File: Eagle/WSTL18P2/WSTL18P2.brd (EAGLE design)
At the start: 23.2 x 23.2 mm, 22 parts, among them CON1 1X6CONN-1.27-ROUND, CON2 1X6CONN-1.27-ROUND, CON3 1X6CONN-1.27-ROUND, CON4 1X6CONN-1.27-ROUND, T1 ABS07AIG

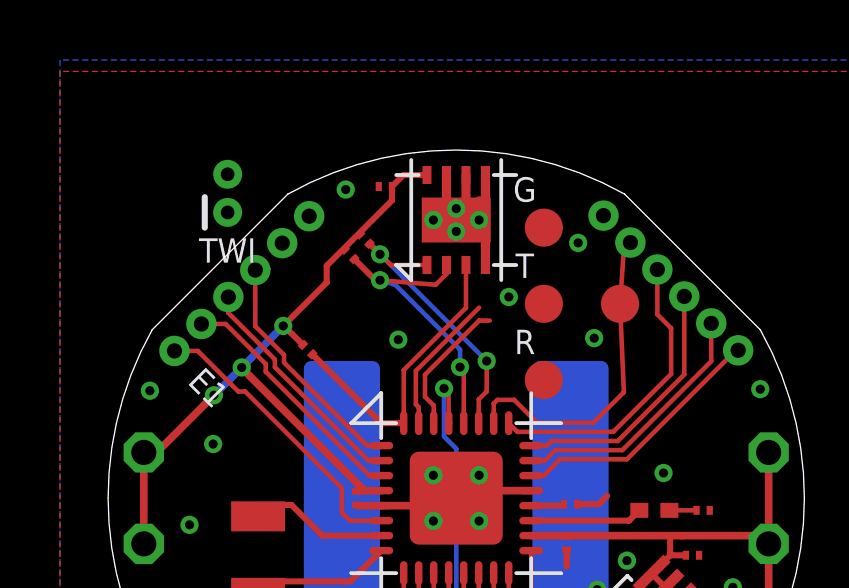
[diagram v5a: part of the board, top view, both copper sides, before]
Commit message: Made TWI (I2C) available on perimeter 1.27mm headers
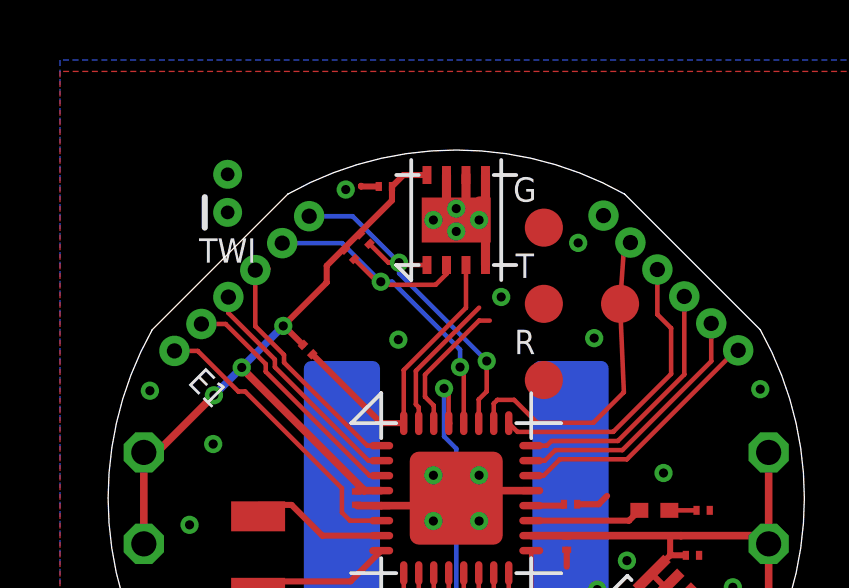
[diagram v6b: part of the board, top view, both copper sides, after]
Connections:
- net SCL0: now also CON4.2
- net SDA0: now also CON4.1
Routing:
- net SCL0: track 9.91 -> 13.8 mm
- net SDA0: track 9.42 -> 12.5 mm
- net GND: track 13.7 -> 14.3 mm
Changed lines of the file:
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@@
 <wire x1="7.3152" y1="17.8054" x2="7.3152" y2="17.7038" width="0.1524" layer="51"/>
 <wire x1="6.8072" y1="18.415" x2="6.9342" y2="18.288" width="0.1524" layer="51"/>
-<wire x1="10.795" y1="20.9042" x2="10.5156" y2="20.9042" width="0.254" layer="51"/>
+<wire x1="11.303" y1="20.447" x2="11.049" y2="20.701" width="0.254" layer="51"/>
 </plain>
 <attributes>
@@
 <contactref element="R2" pad="2"/>
 <via x="14.224" y="17.78" extent="1-16" drill="0.3048" shape="octagon"/>
-<wire x1="14.224" y1="17.78" x2="10.668" y2="21.336" width="0.1524" layer="16"/>
-<wire x1="12.233" y1="20.979" x2="11.025" y2="20.979" width="0.1524" layer="1"/>
+<wire x1="14.224" y1="17.78" x2="11.303" y2="20.701" width="0.1524" layer="16"/>
 <wire x1="13.958" y1="15.708" x2="13.958" y2="16.498" width="0.1524" layer="1"/>
 <wire x1="13.958" y1="16.498" x2="14.224" y2="16.764" width="0.1524" layer="1"/>
 <wire x1="14.224" y1="16.764" x2="14.224" y2="17.78" width="0.1524" layer="1"/>
-<via x="10.668" y="21.336" extent="1-16" drill="0.3048" shape="octagon"/>
-<wire x1="10.668" y1="21.336" x2="11.025" y2="20.979" width="0.1524" layer="1"/>
-<wire x1="10.668" y1="21.336" x2="10.315565625" y2="21.688434375" width="0.2032" layer="1"/>
+<via x="11.303" y="21.0566" extent="1-16" drill="0.3048" shape="octagon"/>
 <wire x1="10.315565625" y1="21.688434375" x2="10.3155625" y2="21.688434375" width="0.2032" layer="1"/>
+<contactref element="CON4" pad="1"/>
+<wire x1="12.233" y1="20.979" x2="11.3806" y2="20.979" width="0.1524" layer="1"/>
+<wire x1="11.3806" y1="20.979" x2="11.303" y2="21.0566" width="0.1524" layer="1"/>
+<wire x1="11.303" y1="20.701" x2="11.303" y2="21.0566" width="0.1524" layer="16"/>
+<wire x1="11.303" y1="21.0566" x2="9.7536" y2="22.606" width="0.1524" layer="16"/>
+<wire x1="9.7536" y1="22.606" x2="8.3058" y2="22.606" width="0.1524" layer="16"/>
+<wire x1="10.3155625" y1="21.688434375" x2="10.947396875" y2="21.0566" width="0.1524" layer="1"/>
+<wire x1="10.947396875" y1="21.0566" x2="11.303" y2="21.0566" width="0.1524" layer="1"/>
 </signal>
 <signal name="SCL0" class="2">
@@
 <contactref element="TMP" pad="2"/>
 <wire x1="13.458" y1="15.708" x2="13.458" y2="17.4538" width="0.1524" layer="1"/>
-<wire x1="12.883" y1="20.6808" x2="12.883" y2="20.979" width="0.1524" layer="1"/>
 <contactref element="R3" pad="2"/>
 <wire x1="13.458" y1="17.4538" x2="13.335" y2="17.5768" width="0.1524" layer="1"/>
 <via x="13.335" y="17.5768" extent="1-16" drill="0.3048" shape="octagon"/>
 <wire x1="13.335" y1="17.5768" x2="13.335" y2="18.161" width="0.1524" layer="16"/>
-<wire x1="13.335" y1="18.161" x2="11.176" y2="20.32" width="0.1524" layer="16"/>
-<wire x1="12.5222" y1="20.32" x2="12.883" y2="20.6808" width="0.1524" layer="1"/>
-<via x="10.668" y="20.4724" extent="1-16" drill="0.3048" shape="octagon"/>
-<wire x1="10.668" y1="20.4724" x2="11.176" y2="20.32" width="0.1524" layer="16"/>
-<wire x1="12.5222" y1="20.32" x2="10.668" y2="20.4724" width="0.1524" layer="1"/>
-<wire x1="10.668" y1="20.4724" x2="10.515596875" y2="20.4724" width="0.2032" layer="1"/>
-<wire x1="10.515596875" y1="20.4724" x2="9.8075625" y2="21.180434375" width="0.2032" layer="1"/>
+<wire x1="13.335" y1="18.161" x2="11.0744" y2="20.4216" width="0.1524" layer="16"/>
+<via x="10.6934" y="20.4216" extent="1-16" drill="0.3048" shape="octagon"/>
+<contactref element="CON4" pad="2"/>
+<wire x1="12.883" y1="20.979" x2="12.883" y2="20.6808" width="0.1524" layer="1"/>
+<wire x1="12.883" y1="20.6808" x2="12.5222" y2="20.32" width="0.1524" layer="1"/>
+<wire x1="12.5222" y1="20.32" x2="10.795" y2="20.32" width="0.1524" layer="1"/>
+<wire x1="10.795" y1="20.32" x2="10.6934" y2="20.4216" width="0.1524" layer="1"/>
+<wire x1="11.0744" y1="20.4216" x2="10.6934" y2="20.4216" width="0.1524" layer="16"/>
+<wire x1="10.6934" y1="20.4216" x2="9.407028125" y2="21.707971875" width="0.1524" layer="16"/>
+<wire x1="9.407028125" y1="21.707971875" x2="7.407771875" y2="21.707971875" width="0.1524" layer="16"/>
+<wire x1="9.8075625" y1="21.180434375" x2="10.566396875" y2="20.4216" width="0.1524" layer="1"/>
+<wire x1="10.566396875" y1="20.4216" x2="10.6934" y2="20.4216" width="0.1524" layer="1"/>
 </signal>
 <signal name="RESET" class="2">
@@
 <wire x1="13.97" y1="13.458" x2="13.97" y2="13.97" width="0.254" layer="1"/>
 <via x="6.9088" y="8.3312" extent="1-16" drill="0.3048"/>
-<via x="14.9606" y="19.9136" extent="1-16" drill="0.3048"/>
+<via x="14.7066" y="19.9136" extent="1-16" drill="0.3048"/>
 <wire x1="12.446" y1="12.958" x2="12.696" y2="13.208" width="0.254" layer="1"/>
 <wire x1="12.696" y1="13.208" x2="13.208" y2="13.208" width="0.254" layer="1"/>
@@
 <wire x1="9.9106" y1="12.958" x2="10.708" y2="12.958" width="0.254" layer="1"/>
 <wire x1="9.8806" y1="12.988" x2="9.9106" y2="12.958" width="0.2032" layer="1"/>
-<wire x1="9.525" y1="23.495" x2="10.6258" y2="23.5966" width="0" layer="19" extent="1-1"/>
-<wire x1="21.302" y1="11.303" x2="22.4282" y2="10.2362" width="0" layer="19" extent="1-1"/>
-<wire x1="21.6576" y1="12.8016" x2="21.302" y2="11.303" width="0" layer="19" extent="1-1"/>
+<wire x1="10.6258" y1="23.5966" x2="10.033" y2="23.5966" width="0.2032" layer="1"/>
+<wire x1="10.033" y1="23.5966" x2="10.033" y2="23.622" width="0.2032" layer="1"/>
+<wire x1="21.302" y1="11.303" x2="21.6576" y2="12.8016" width="0" layer="19" extent="1-1"/>
+<wire x1="22.4282" y1="10.2362" x2="21.302" y2="11.303" width="0" layer="19" extent="1-1"/>
 </signal>
 <signal name="AREF">

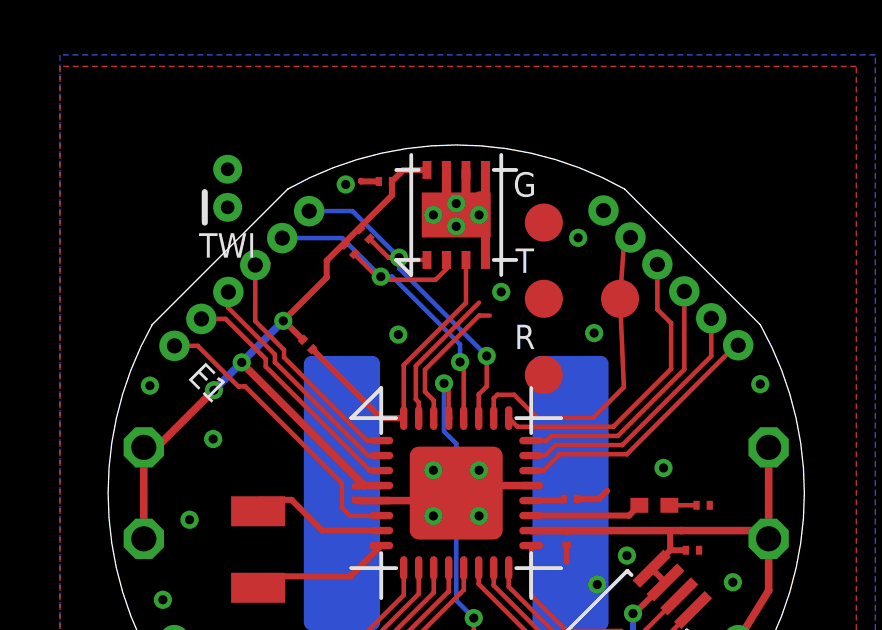
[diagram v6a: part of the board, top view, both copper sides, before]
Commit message: More work on TWI (I2C) traces
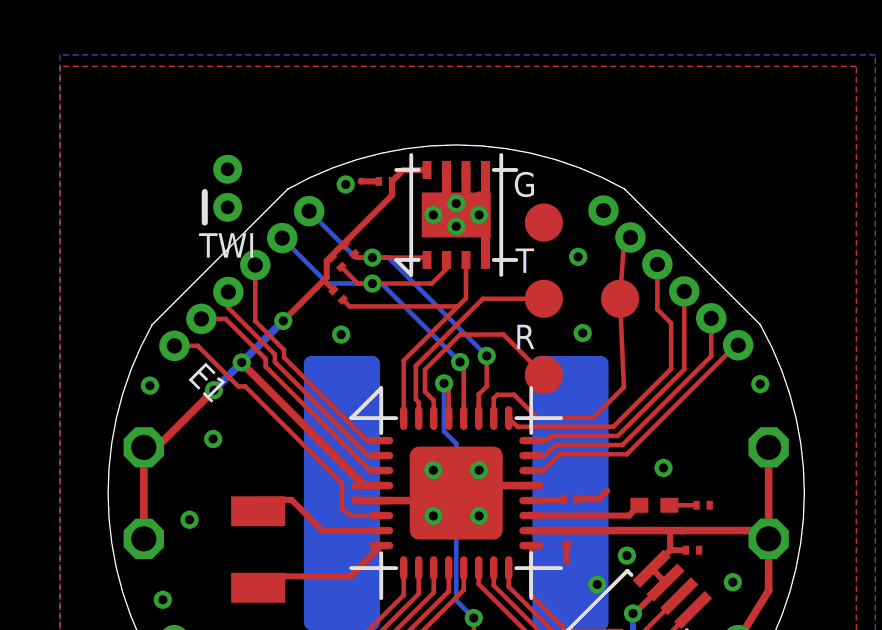
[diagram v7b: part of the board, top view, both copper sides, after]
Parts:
- moved R4 1.94 mm to (9.27, 19.8)
- moved R2 0.72 mm to (9.65, 21.3)
- moved R3 0.61 mm to (9.22, 20.9)
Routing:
- net TXD0: track 4.76 -> 6.97 mm
- net RXD0: track 4.64 -> 6.74 mm
- net GND: vias 27 -> 26

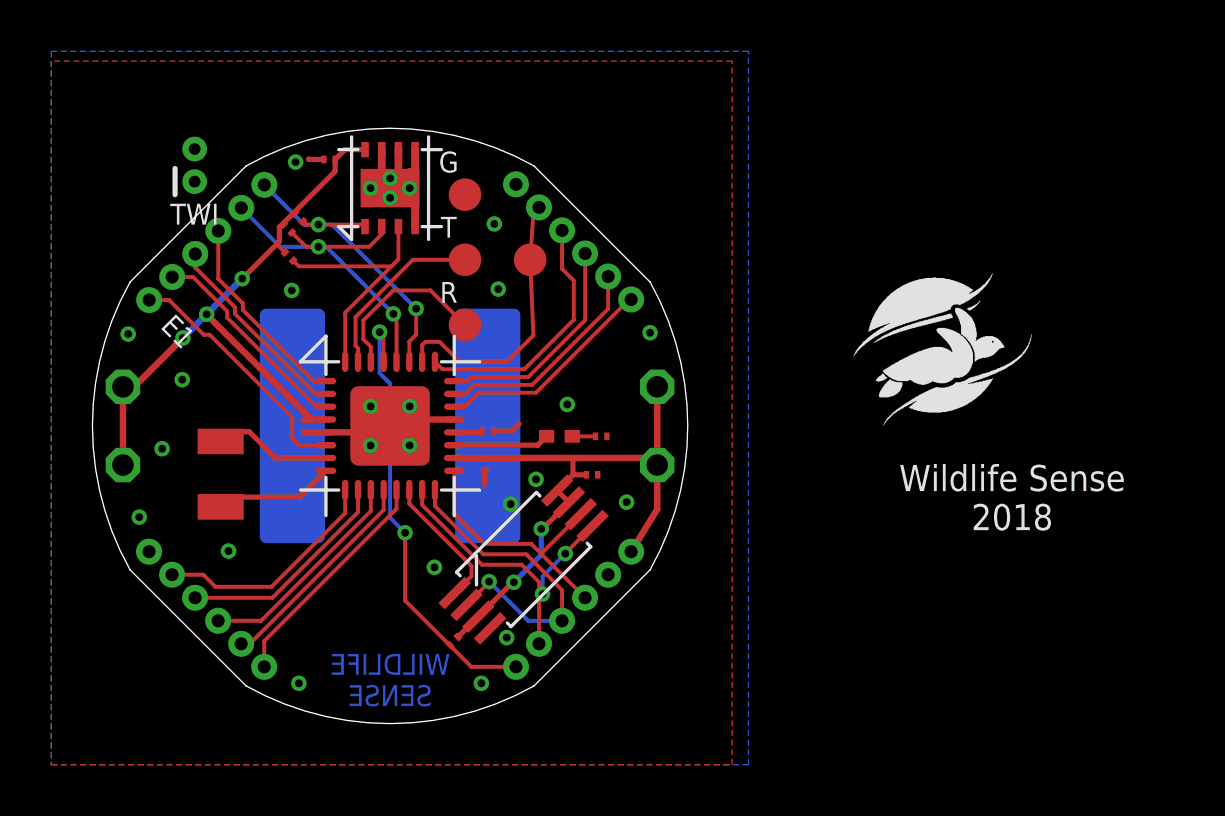
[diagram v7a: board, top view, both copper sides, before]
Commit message: Added pads on the positive battery holder contacts
This will allow use of both SMD and through-hole versions of the battery holder
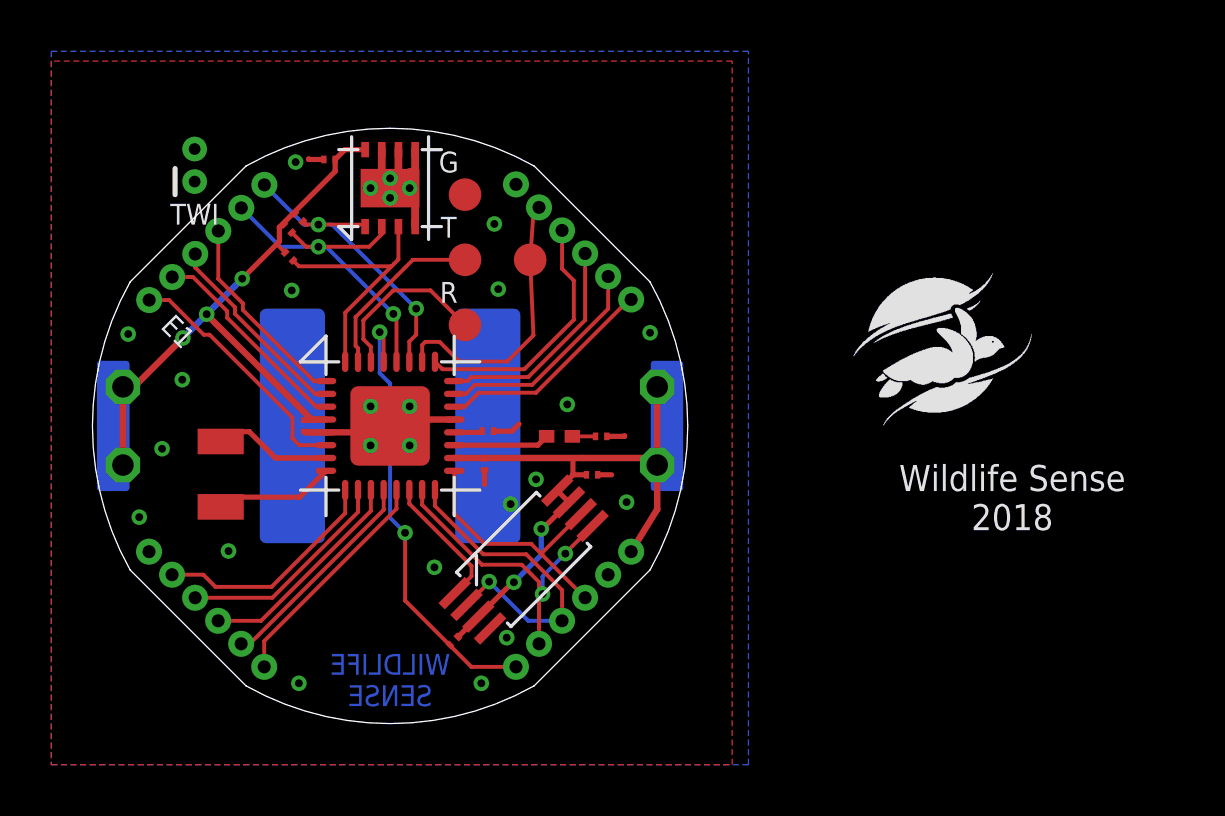
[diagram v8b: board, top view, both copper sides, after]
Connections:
- net VCC: now also U$1.BATT5, U$1.BATT6
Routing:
- net GND: track 14.3 -> 15.5 mm
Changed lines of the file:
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@@
 <wire x1="9.115434375" y1="19.9675625" x2="9.115434375" y2="19.967565625" width="0.1524" layer="1"/>
 <wire x1="9.115434375" y1="19.967565625" x2="8.7884" y2="20.2946" width="0.1524" layer="1"/>
-<wire x1="9.064634375" y1="21.0597625" x2="9.496434375" y2="21.4915625" width="0" layer="19" extent="1-1"/>
-<wire x1="8.89" y1="20.955" x2="9.064634375" y2="21.0597625" width="0" layer="19" extent="1-1"/>
-<wire x1="15.708" y1="11.958" x2="10.708" y2="13.458" width="0" layer="19" extent="1-1"/>
+<contactref element="U$1" pad="BATT5"/>
+<contactref element="U$1" pad="BATT6"/>
+<wire x1="23.348" y1="11.958" x2="24.003" y2="13.208" width="0" layer="19" extent="1-16"/>
+<wire x1="10.708" y1="13.458" x2="15.708" y2="11.958" width="0" layer="19" extent="1-1"/>
+<wire x1="9.064634375" y1="21.0597625" x2="8.89" y2="20.955" width="0" layer="19" extent="1-1"/>
+<wire x1="9.496434375" y1="21.4915625" x2="9.064634375" y2="21.0597625" width="0" layer="19" extent="1-1"/>
+<wire x1="2.413" y1="13.208" x2="2.794" y2="14.732" width="0" layer="19" extent="16-16"/>
 </signal>
 <signal name="GND" class="1">
@@
 <wire x1="10.708" y1="12.958" x2="12.446" y2="12.958" width="0.254" layer="1"/>
 <wire x1="12.446" y1="12.958" x2="12.446" y2="12.446" width="0.254" layer="1"/>
-<wire x1="15.708" y1="13.458" x2="13.97" y2="13.458" width="0.254" layer="1"/>
 <wire x1="13.97" y1="13.458" x2="13.97" y2="13.97" width="0.254" layer="1"/>
 <via x="6.9088" y="8.3312" extent="1-16" drill="0.3048"/>
@@
 <wire x1="10.6258" y1="23.5966" x2="10.033" y2="23.5966" width="0.2032" layer="1"/>
 <wire x1="10.033" y1="23.5966" x2="10.033" y2="23.622" width="0.2032" layer="1"/>
-<wire x1="21.302" y1="11.303" x2="21.6576" y2="12.8016" width="0" layer="19" extent="1-1"/>
-<wire x1="22.4282" y1="10.2362" x2="21.302" y2="11.303" width="0" layer="19" extent="1-1"/>
+<wire x1="21.302" y1="11.303" x2="21.844" y2="11.303" width="0.2032" layer="1"/>
+<wire x1="21.6576" y1="12.8016" x2="22.352" y2="12.8016" width="0.2032" layer="1"/>
+<wire x1="22.352" y1="12.8016" x2="22.352" y2="12.827" width="0.2032" layer="1"/>
+<wire x1="15.708" y1="13.458" x2="13.97" y2="13.458" width="0.254" layer="1"/>
 </signal>
 <signal name="AREF">
